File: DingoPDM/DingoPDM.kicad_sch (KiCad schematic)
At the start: 6 parts

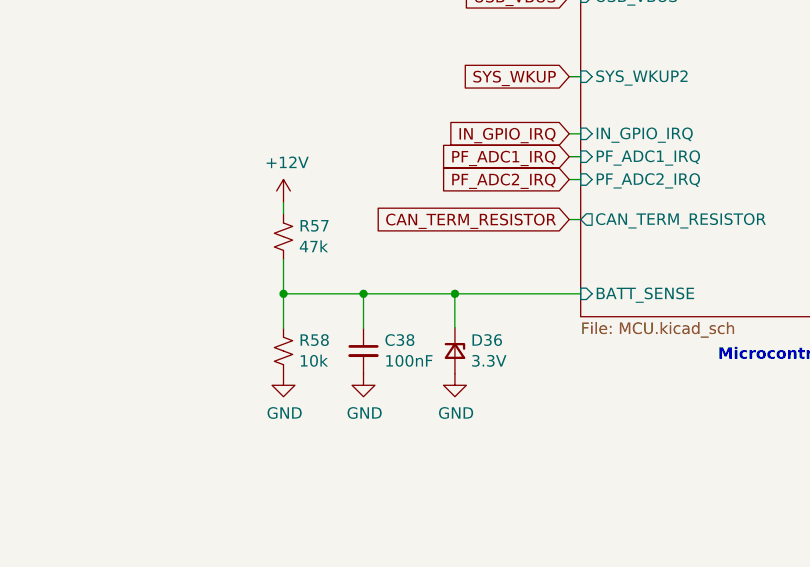
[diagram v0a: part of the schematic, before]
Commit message: Swapped to AMPSEAL 14 pins
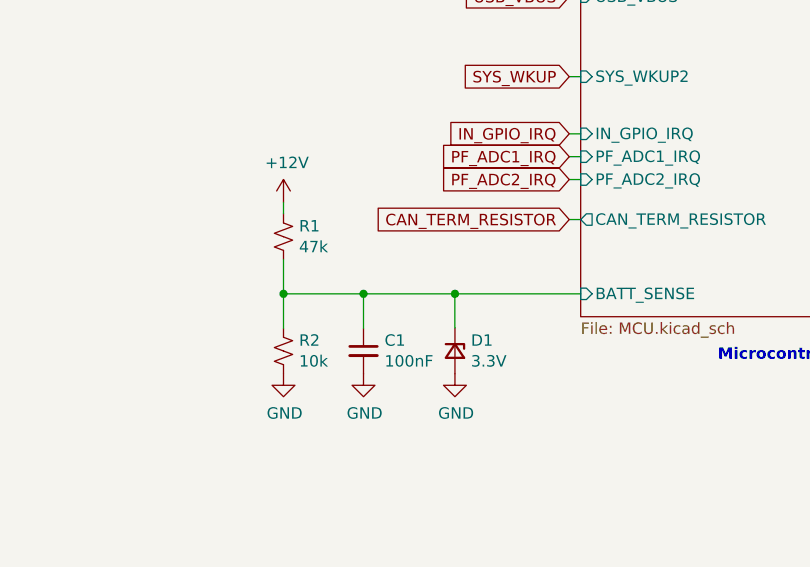
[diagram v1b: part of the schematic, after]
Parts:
- renumbered C38 to C1, D36 to D1, R57 to R1, R58 to R2

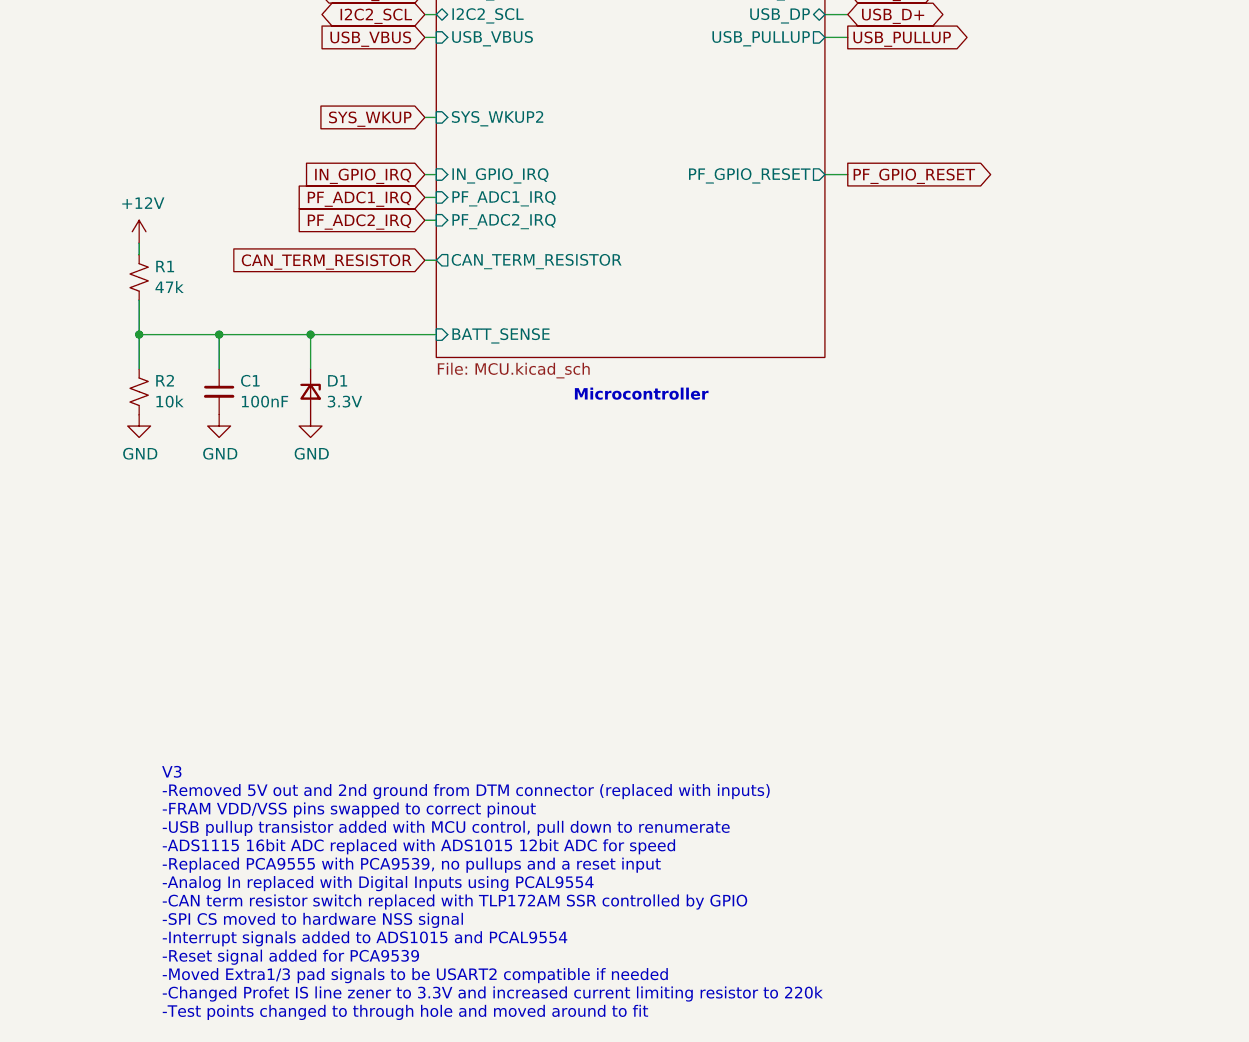
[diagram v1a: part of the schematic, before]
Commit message: Removed unused IRQs, added pd res on PF GPIO reset
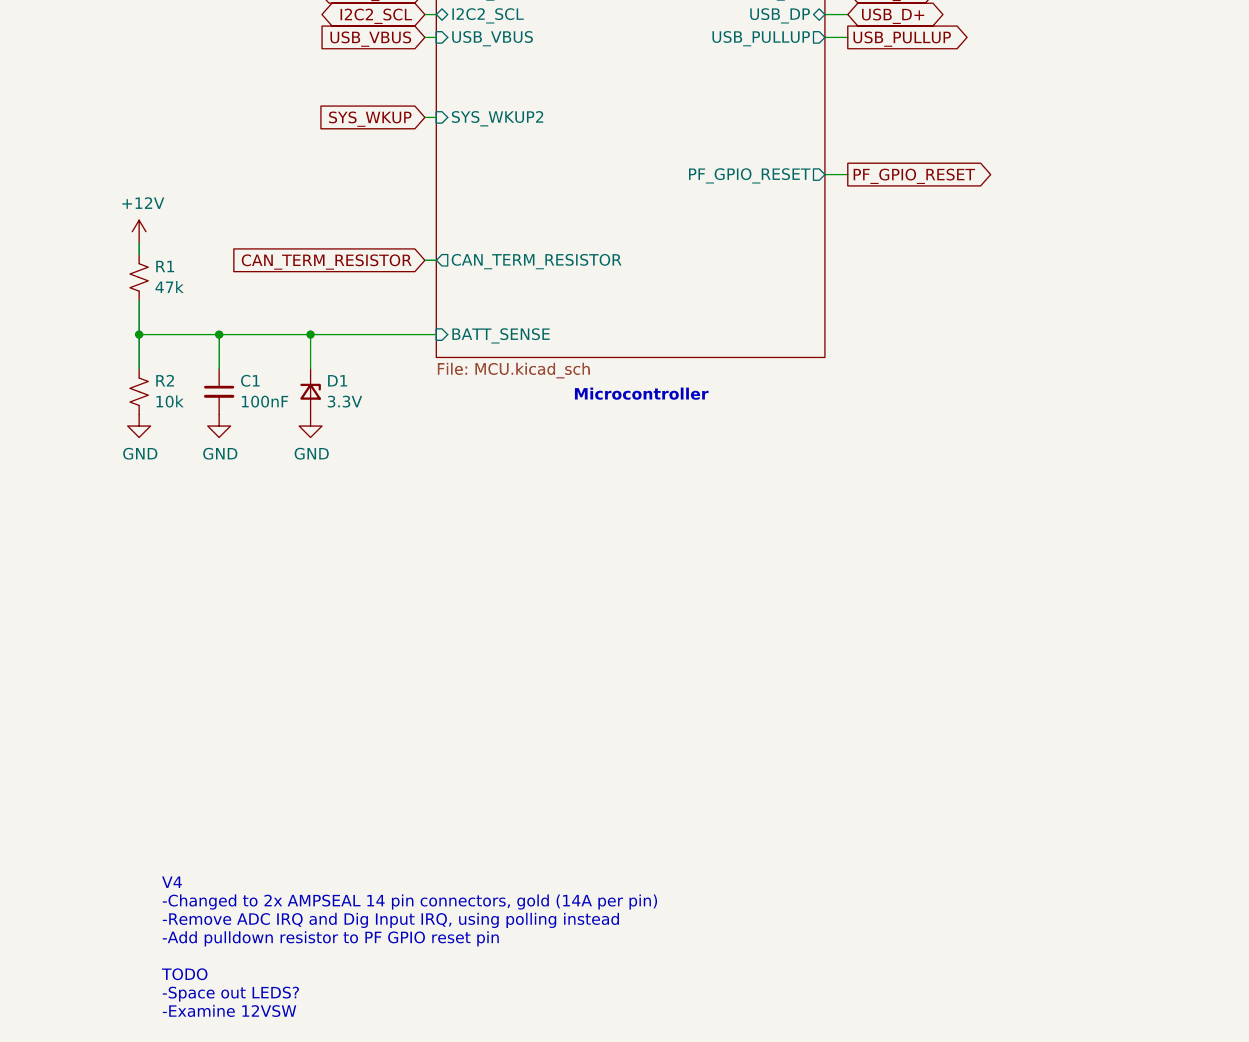
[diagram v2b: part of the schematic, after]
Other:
- sheet MCU ports: added none; removed IN_GPIO_IRQ, PF_ADC1_IRQ, PF_ADC2_IRQ
- note added: "V4 -Changed to 2x AMPSEAL 14 pin connectors, gold (14A per pin) -Remove ADC IRQ and Dig Input IRQ, using polling instead -Add pulldown resistor to PF GPIO reset pin TODO -Space out LEDS? -Examine 12VSW"
- note removed: "V3 -Removed 5V out and 2nd ground from DTM connector (replaced with inputs) -FRAM VDD/VSS pins swapped to correct pinout -USB pullup transistor added with MCU control, pull down to renumerate -ADS1115 16bit ADC replaced with ADS1015 12bit ADC for speed -Replaced PCA9555 with PCA9539, no pullups and a reset input -Analog In replaced with Digital Inputs using PCAL9554 -CAN term resistor switch repl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"

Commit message: Moved folders
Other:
- note added: "V4 -Changed to 2x AMPSEAL 14 pin connectors, gold (14A per pin) -Remove ADC IRQ and Dig Input IRQ, using polling instead -Add pulldown resistor to PF GPIO reset pin TODO -Space out LEDS?"
- note removed: "V4 -Changed to 2x AMPSEAL 14 pin connectors, gold (14A per pin) -Remove ADC IRQ and Dig Input IRQ, using polling instead -Add pulldown resistor to PF GPIO reset pin TODO -Space out LEDS? -Examine 12VSW"
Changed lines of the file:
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@@
     (effects (font (size 1.27 1.27) (thickness 0.254) bold) (justify left bottom))
   )
-  (text "V4\n-Changed to 2x AMPSEAL 14 pin connectors, gold (14A per pin)\n-Remove ADC IRQ and Dig Input IRQ, using polling instead \n-Add pulldown resistor to PF GPIO reset pin\n\nTODO\n-Space out LEDS?\n-Examine 12VSW"
+  (text "V4\n-Changed to 2x AMPSEAL 14 pin connectors, gold (14A per pin)\n-Remove ADC IRQ and Dig Input IRQ, using polling instead \n-Add pulldown resistor to PF GPIO reset pin\n\nTODO\n-Space out LEDS?"
     (at 86.995 189.23 0)
     (effects (font (size 1.27 1.27)) (justify left bottom))
@@
     )
     (path "/00000000-0000-0000-0000-00005f4db108/00000000-0000-0000-0000-00005f4e276a"
-      (reference "Y1") (unit 1) (value "8mHz") (footprint "Crystal:Crystal_SMD_5032-2Pin_5.0x3.2mm")
+      (reference "Y1") (unit 1) (value "8mHz") (footprint "Crystals_Modify:Crystal_SMD_5032-2Pin_5.0x3.2mm_HandSoldering")
     )
     (path "/00000000-0000-0000-0000-00005f4db108/00000000-0000-0000-0000-00005f6286d5"
-      (reference "Y2") (unit 1) (value "32.768kHz") (footprint "Crystal:Crystal_SMD_3215-2Pin_3.2x1.5mm")
-    )
-  )
+      (reference "Y2") (unit 1) (value "32.768kHz") (footprint "Crystals_Modify:Crystal_SMD_3215-2Pin_3.2x1.5mm_HandSoldering")
+    )
+  )

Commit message: V5 changes
Changed tracks/clearances/DRC to meet JLCPCB 2oz rules. Changed on switch to 12V input. Switched to TagConnect
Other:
- note added: "V5 -Changed PCB to fit JLCPCB 2oz rules -Changed on switch input to 12V in -Switched to TagConnect TC2030"
- note removed: "V4 -Changed to 2x AMPSEAL 14 pin connectors, gold (14A per pin) -Remove ADC IRQ and Dig Input IRQ, using polling instead -Add pulldown resistor to PF GPIO reset pin TODO -Space out LEDS?"

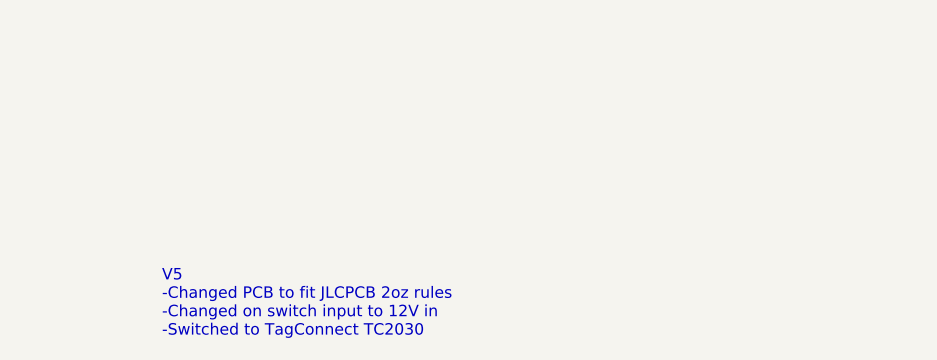
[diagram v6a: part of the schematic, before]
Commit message: V5 As Built
-Changed ADS1015 to MAX11613EUA+T due to supply issues
-Changed PCB to match JLCPCB 2oz rules
-Changed ON_SW input to 12V switched
-Switched to TagConnect TC2030
-Changed pin positions of GND, IN1, IN2
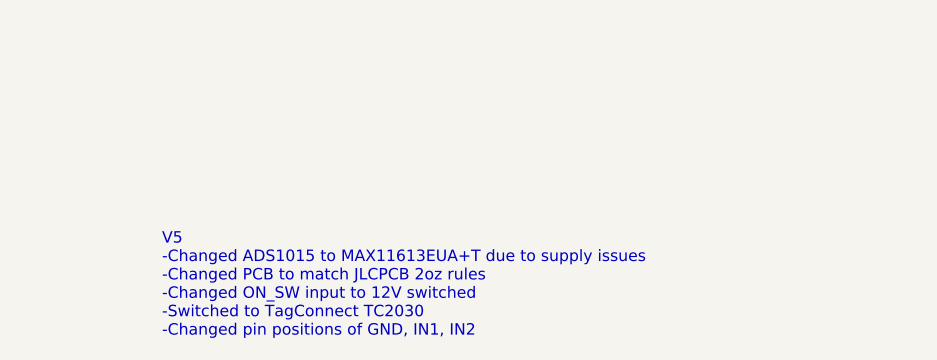
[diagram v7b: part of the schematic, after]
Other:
- note added: "V5 -Changed ADS1015 to MAX11613EUA+T due to supply issues -Changed PCB to match JLCPCB 2oz rules -Changed ON_SW input to 12V switched -Switched to TagConnect TC2030 -Changed pin positions of GND, IN1, IN2"
- note removed: "V5 -Changed PCB to fit JLCPCB 2oz rules -Changed on switch input to 12V in -Switched to TagConnect TC2030"
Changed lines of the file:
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@@
     (date "2023-02-23")
     (rev "v5")
+    (comment 3 "github.com/corygrant")
     (comment 4 "Cory Grant")
   )
@@
     (effects (font (size 1.27 1.27) (thickness 0.254) bold) (justify left bottom))
   )
-  (text "V5\n-Changed PCB to fit JLCPCB 2oz rules\n-Changed on switch input to 12V in\n-Switched to TagConnect TC2030\n"
+  (text "V5\n-Changed ADS1015 to MAX11613EUA+T due to supply issues\n-Changed PCB to match JLCPCB 2oz rules\n-Changed ON_SW input to 12V switched\n-Switched to TagConnect TC2030\n-Changed pin positions of GND, IN1, IN2"
     (at 86.995 189.23 0)
     (effects (font (size 1.27 1.27)) (justify left bottom))
@@
     (instances
       (project "DingoPDM"
+        (path "/8948e307-9174-4227-9c28-3ff885e6e83d" (page "4"))
+      )
+    )
+  )
+  (sheet (at 255.27 17.78) (size 22.86 21.59) (fields_autoplaced)
+    (stroke (width 0) (type solid))
+    (fill (color 0 0 0 0.0000))
+    (property "Sheetname" "HighCurrentDrivers" (at 255.27 17.0684 0)
+      (effects (font (size 1.27 1.27)) (justify left bottom))
+    )
+    (property "Sheetfile" "HighCurrentDrivers.kicad_sch" (at 255.27 39.9546 0)
+      (effects (font (size 1.27 1.27)) (justify left top))
+    )
+    (instances
+      (project "DingoPDM"
         (path "/8948e307-9174-4227-9c28-3ff885e6e83d" (page "7"))
       )
     )
   )
-  (sheet (at 255.27 17.78) (size 22.86 21.59) (fields_autoplaced)
-    (stroke (width 0) (type solid))
-    (fill (color 0 0 0 0.0000))
-    (property "Sheetname" "HighCurrentDrivers" (at 255.27 17.0684 0)
-      (effects (font (size 1.27 1.27)) (justify left bottom))
-    )
-    (property "Sheetfile" "HighCurrentDrivers.kicad_sch" (at 255.27 39.9546 0)
-      (effects (font (size 1.27 1.27)) (justify left top))
-    )
-    (instances
-      (project "DingoPDM"
-        (path "/8948e307-9174-4227-9c28-3ff885e6e83d" (page "4"))
-      )
-    )
-  )
   (sheet (at 255.27 49.53) (size 22.86 21.59) (fields_autoplaced)
     (stroke (width 0) (type solid))
@@
     (instances
       (project "DingoPDM"
+        (path "/8948e307-9174-4227-9c28-3ff885e6e83d" (page "12"))
+      )
+    )
+  )
+  (sheet (at 15.24 46.355) (size 22.86 21.59) (fields_autoplaced)
+    (stroke (width 0) (type solid))
+    (fill (color 0 0 0 0.0000))
+    (property "Sheetname" "Connectors" (at 15.24 45.6434 0)
+      (effects (font (size 1.27 1.27)) (justify left bottom))
+    )
+    (property "Sheetfile" "Connectors.kicad_sch" (at 15.24 68.5296 0)
+      (effects (font (size 1.27 1.27)) (justify left top))
+    )
+    (instances
+      (project "DingoPDM"
+        (path "/8948e307-9174-4227-9c28-3ff885e6e83d" (page "3"))
+      )
+    )
+  )
+  (sheet (at 14.605 116.84) (size 22.86 21.59) (fields_autoplaced)
+    (stroke (width 0) (type solid))
+    (fill (color 0 0 0 0.0000))
+    (property "Sheetname" "I2C" (at 14.605 116.1284 0)
+      (effects (font (size 1.27 1.27)) (justify left bottom))
+    )
+    (property "Sheetfile" "I2C.kicad_sch" (at 14.605 139.0146 0)
+      (effects (font (size 1.27 1.27)) (justify left top))
+    )
+    (instances
+      (project "DingoPDM"
+        (path "/8948e307-9174-4227-9c28-3ff885e6e83d" (page "5"))
+      )
+    )
+  )
+  (sheet (at 15.24 15.875) (size 22.86 21.59) (fields_autoplaced)
+    (stroke (width 0) (type solid))
+    (fill (color 0 0 0 0.0000))
+    (property "Sheetname" "Power" (at 15.24 15.1634 0)
+      (effects (font (size 1.27 1.27)) (justify left bottom))
+    )
+    (property "Sheetfile" "Power.kicad_sch" (at 15.24 38.0496 0)
+      (effects (font (size 1.27 1.27)) (justify left top))
+    )
+    (instances
+      (project "DingoPDM"
+        (path "/8948e307-9174-4227-9c28-3ff885e6e83d" (page "2"))
+      )
+    )
+  )
+  (sheet (at 14.605 144.145) (size 22.86 21.59) (fields_autoplaced)
+    (stroke (width 0) (type solid))
+    (fill (color 0 0 0 0.0000))
+    (property "Sheetname" "DigitalInputs" (at 14.605 143.4334 0)
+      (effects (font (size 1.27 1.27)) (justify left bottom))
+    )
+    (property "Sheetfile" "DigIn.kicad_sch" (at 14.605 166.3196 0)
+      (effects (font (size 1.27 1.27)) (justify left top))
+    )
+    (instances
+      (project "DingoPDM"
         (path "/8948e307-9174-4227-9c28-3ff885e6e83d" (page "6"))
       )
     )
-  )
-  (sheet (at 15.24 46.355) (size 22.86 21.59) (fields_autoplaced)
-    (stroke (width 0) (type solid))
-    (fill (color 0 0 0 0.0000))
-    (property "Sheetname" "Connectors" (at 15.24 45.6434 0)
-      (effects (font (size 1.27 1.27)) (justify left bottom))
-    )
-    (property "Sheetfile" "Connectors.kicad_sch" (at 15.24 68.5296 0)
-      (effects (font (size 1.27 1.27)) (justify left top))
-    )
-    (instances
-      (project "DingoPDM"
-        (path "/8948e307-9174-4227-9c28-3ff885e6e83d" (page "2"))
-      )
-    )
-  )
-  (sheet (at 14.605 116.84) (size 22.86 21.59) (fields_autoplaced)
-    (stroke (width 0) (type solid))
-    (fill (color 0 0 0 0.0000))
-    (property "Sheetname" "I2C" (at 14.605 116.1284 0)
-      (effects (font (size 1.27 1.27)) (justify left bottom))
-    )
-    (property "Sheetfile" "I2C.kicad_sch" (at 14.605 139.0146 0)
-      (effects (font (size 1.27 1.27)) (justify left top))
-    )
-    (instances
-      (project "DingoPDM"
-        (path "/8948e307-9174-4227-9c28-3ff885e6e83d" (page "5"))
-      )
-    )
-  )
-  (sheet (at 15.24 15.875) (size 22.86 21.59) (fields_autoplaced)
-    (stroke (width 0) (type solid))
-    (fill (color 0 0 0 0.0000))
-    (property "Sheetname" "Power" (at 15.24 15.1634 0)
-      (effects (font (size 1.27 1.27)) (justify left bottom))
-    )
-    (property "Sheetfile" "Power.kicad_sch" (at 15.24 38.0496 0)
-      (effects (font (size 1.27 1.27)) (justify left top))
-    )
-    (instances
-      (project "DingoPDM"
-        (path "/8948e307-9174-4227-9c28-3ff885e6e83d" (page "8"))
-      )
-    )
-  )
-  (sheet (at 14.605 144.145) (size 22.86 21.59) (fields_autoplaced)
-    (stroke (width 0) (type solid))
-    (fill (color 0 0 0 0.0000))
-    (property "Sheetname" "DigitalInputs" (at 14.605 143.4334 0)
-      (effects (font (size 1.27 1.27)) (justify left bottom))
-    )
-    (property "Sheetfile" "DigIn.kicad_sch" (at 14.605 166.3196 0)
-      (effects (font (size 1.27 1.27)) (justify left top))
-    )
-    (instances
-      (project "DingoPDM"
-        (path "/8948e307-9174-4227-9c28-3ff885e6e83d" (page "3"))
-      )
-    )

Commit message: Incorrect PN for some diodes and resistors
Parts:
- D1: Digi-Key_PN SZMMSZ4684T1GOSCT-ND -> 1727-5150-1-ND
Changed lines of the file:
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@@
       (effects (font (size 1.27 1.27)) hide)
     )
-    (property "Digi-Key_PN" "SZMMSZ4684T1GOSCT-ND" (at 103.505 119.38 0)
+    (property "Digi-Key_PN" "1727-5150-1-ND" (at 103.505 119.38 0)
       (effects (font (size 1.27 1.27)) hide)
     )
